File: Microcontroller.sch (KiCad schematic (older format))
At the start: 15 parts

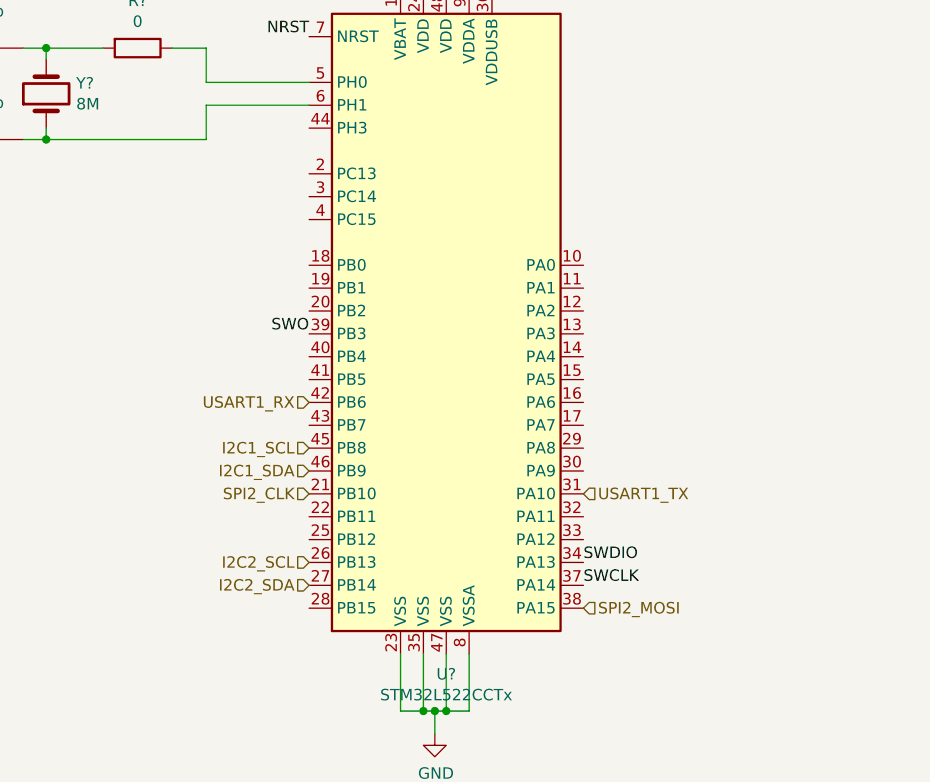
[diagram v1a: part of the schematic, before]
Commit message: added rj45 input
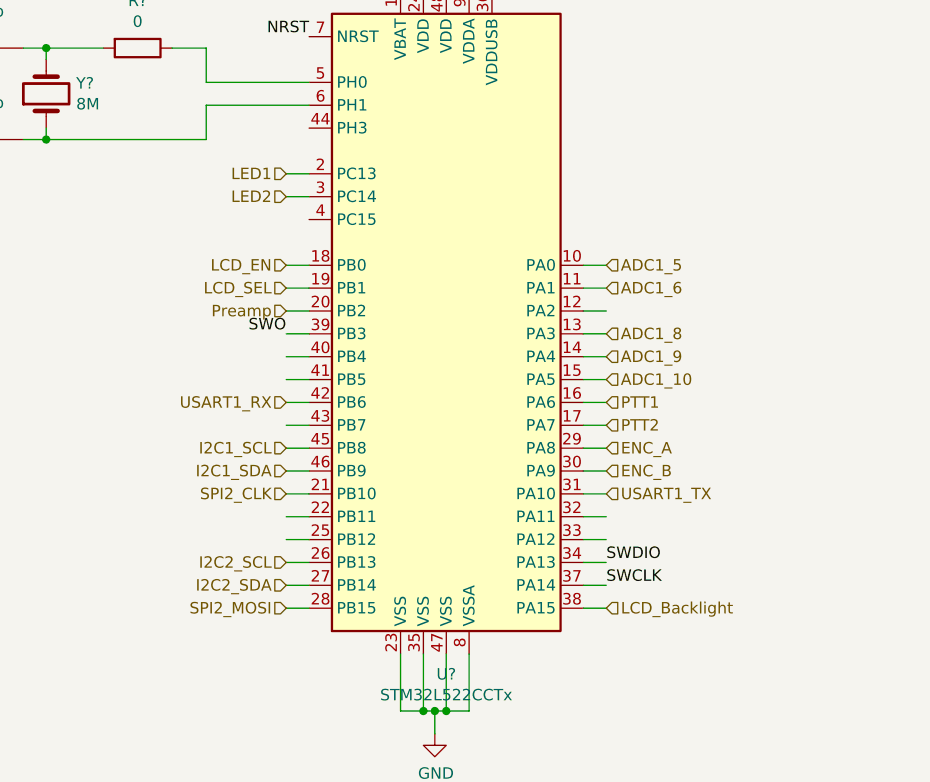
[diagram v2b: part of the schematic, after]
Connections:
- net labels added: ADC1_10, ADC1_5, ADC1_6, ADC1_8, ADC1_9, ENC_A, ENC_B, LCD_Backlight, LCD_EN, LCD_SEL, LED1, LED2, PTT1, PTT2, Preamp
- wire segments 61 -> 95
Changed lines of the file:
@@
 $Descr A4 11693 8268
 encoding utf-8
-Sheet 3 6
+Sheet 3 7
 Title ""
 Date ""
@@
 Text Label 4550 2350 2    50   ~ 0
 NRST
-Text Label 4550 3650 2    50   ~ 0
+Text Label 4450 3650 2    50   ~ 0
 SWO
-Text Label 5750 4650 0    50   ~ 0
+Text Label 5850 4650 0    50   ~ 0
 SWDIO
-Text Label 5750 4750 0    50   ~ 0
+Text Label 5850 4750 0    50   ~ 0
 SWCLK
 Text Label 9550 3150 2    50   ~ 0
@@
 Wire Wire Line
 	9450 3250 9550 3250
-Text HLabel 4550 4150 0    50   Input ~ 0
+Text HLabel 4450 4150 0    50   Input ~ 0
 I2C1_SCL
-Text HLabel 4550 4250 0    50   Input ~ 0
+Text HLabel 4450 4250 0    50   Input ~ 0
 I2C1_SDA
-Text HLabel 4550 4650 0    50   Input ~ 0
+Text HLabel 4450 4650 0    50   Input ~ 0
 I2C2_SCL
-Text HLabel 4550 4750 0    50   Input ~ 0
+Text HLabel 4450 4750 0    50   Input ~ 0
 I2C2_SDA
-Text HLabel 5750 4350 2    50   Input ~ 0
+Text HLabel 5850 4350 2    50   Input ~ 0
 USART1_TX
 Wire Wire Line
 	5350 1750 5350 2150
-Text HLabel 4550 3950 0    50   Input ~ 0
+Text HLabel 4450 3950 0    50   Input ~ 0
 USART1_RX
-Text HLabel 5750 4850 2    50   Input ~ 0
+Text HLabel 4450 4850 0    50   Input ~ 0
 SPI2_MOSI
-Text HLabel 4550 4350 0    50   Input ~ 0
+Text HLabel 4450 4350 0    50   Input ~ 0
 SPI2_CLK
 $Comp
@@
 Wire Wire Line
 	3400 2800 4100 2800
+Text HLabel 4450 2950 0    50   Input ~ 0
+LED1
+Text HLabel 4450 3050 0    50   Input ~ 0
+LED2
+Text HLabel 5850 4150 2    50   Input ~ 0
+ENC_A
+Text HLabel 5850 4250 2    50   Input ~ 0
+ENC_B
+Wire Wire Line
+	5750 4150 5850 4150
+Wire Wire Line
+	5750 4250 5850 4250
+Wire Wire Line
+	5750 4850 5850 4850
+Wire Wire Line
+	4450 3350 4550 3350
+Wire Wire Line
+	4450 3450 4550 3450
+Wire Wire Line
+	4450 3550 4550 3550
+Wire Wire Line
+	4450 3650 4550 3650
+Wire Wire Line
+	4450 3750 4550 3750
+Wire Wire Line
+	4450 3850 4550 3850
+Wire Wire Line
+	4450 3950 4550 3950
+Wire Wire Line
+	4450 4050 4550 4050
+Wire Wire Line
+	4450 4150 4550 4150
+Wire Wire Line
+	4450 4250 4550 4250
+Wire Wire Line
+	4450 4350 4550 4350
+Wire Wire Line
+	4450 4450 4550 4450
+Wire Wire Line
+	4450 4550 4550 4550
+Wire Wire Line
+	4450 4650 4550 4650
+Wire Wire Line
+	4450 4750 4550 4750
+Wire Wire Line
+	4450 4850 4550 4850
+Wire Wire Line
+	5850 3350 5750 3350
+Wire Wire Line
+	5850 3450 5750 3450
+Wire Wire Line
+	5850 3550 5750 3550
+Wire Wire Line
+	5850 3650 5750 3650
+Wire Wire Line
+	5850 3750 5750 3750
+Wire Wire Line
+	5850 3850 5750 3850
+Wire Wire Line
+	5850 3950 5750 3950
+Wire Wire Line
+	5850 4050 5750 4050
+Wire Wire Line
+	5850 4350 5750 4350
+Wire Wire Line
+	5850 4450 5750 4450
+Wire Wire Line
+	5850 4550 5750 4550
+Wire Wire Line
+	5850 4650 5750 4650
+Wire Wire Line
+	5850 4750 5750 4750
+Text HLabel 5850 3950 2    50   Input ~ 0
+PTT1
+Text HLabel 5850 4050 2    50   Input ~ 0
+PTT2
+Text HLabel 4450 3350 0    50   Input ~ 0
+LCD_EN
+Text HLabel 4450 3450 0    50   Input ~ 0
+LCD_SEL
+Text HLabel 5850 4850 2    50   Input ~ 0
+LCD_Backlight
+Text HLabel 5850 3350 2    50   Input ~ 0
+ADC1_5
+Text HLabel 5850 3450 2    50   Input ~ 0
+ADC1_6
+Text HLabel 5850 3650 2    50   Input ~ 0
+ADC1_8
+Text HLabel 5850 3750 2    50   Input ~ 0
+ADC1_9
+Text HLabel 5850 3850 2    50   Input ~ 0
+ADC1_10
+Wire Wire Line
+	4550 2950 4450 2950
+Wire Wire Line
+	4550 3050 4450 3050
+Text HLabel 4450 3550 0    50   Input ~ 0
+Preamp
 $EndSCHEMATC

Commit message: Ready for layout
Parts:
- removed R?: R, symbol AR2ISS:R
- added C?: 100n, symbol AR2ISS:C
- added JP?: Jumper_NC_Small, symbol Device:Jumper_NC_Small
- added R?: 10k, symbol AR2ISS:R
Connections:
- net labels added: AMP, CREL_A, CREL_B, C_NC, C_NO, PTT_Main, PTT_Sub, ROT_DOWN, ROT_LEFT, ROT_RIGHT, ROT_UP
- net labels removed: I2C2_SCL, I2C2_SDA, PTT1, PTT2
- wire segments 95 -> 105
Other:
- moved on the sheet: J?
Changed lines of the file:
@@
 $Descr A4 11693 8268
 encoding utf-8
-Sheet 3 7
+Sheet 7 9
 Title ""
 Date ""
@@
 	1    0    0    -1
 $EndComp
-$Comp
-L AR2ISS:R R?
-U 1 1 606DF993
-P 7550 1300
-F 0 "R?" H 7620 1346 50  0000 L CNN
-F 1 "R" H 7620 1255 50  0000 L CNN
-F 2 "" V 7480 1300 50  0001 C CNN
-F 3 "~" H 7550 1300 50  0001 C CNN
-	1    7550 1300
-	1    0    0    -1
-$EndComp
 Wire Wire Line
 	4950 1750 4950 2050
@@
 L Connector_Generic:Conn_02x03_Odd_Even J?
 U 1 1 606FEAF1
-P 9750 3150
-F 0 "J?" H 9800 3467 50  0000 C CNN
-F 1 "Conn_02x03_Odd_Even" H 9800 3376 50  0000 C CNN
-F 2 "" H 9750 3150 50  0001 C CNN
-F 3 "~" H 9750 3150 50  0001 C CNN
-	1    9750 3150
+P 8100 2800
+F 0 "J?" H 8150 3117 50  0000 C CNN
+F 1 "Conn_02x03_Odd_Even" H 8150 3026 50  0000 C CNN
+F 2 "" H 8100 2800 50  0001 C CNN
+F 3 "~" H 8100 2800 50  0001 C CNN
+	1    8100 2800
 	1    0    0    -1
 $EndComp
@@
 Text Label 5850 4750 0    50   ~ 0
 SWCLK
-Text Label 9550 3150 2    50   ~ 0
+Text Label 7900 2800 2    50   ~ 0
 NRST
-Text Label 10050 3250 0    50   ~ 0
+Text Label 8400 2900 0    50   ~ 0
 SWO
-Text Label 10050 3050 0    50   ~ 0
+Text Label 8400 2700 0    50   ~ 0
 SWDIO
-Text Label 10050 3150 0    50   ~ 0
+Text Label 8400 2800 0    50   ~ 0
 SWCLK
 $Comp
 L power:GND #PWR?
 U 1 1 60716775
-P 9450 3400
-F 0 "#PWR?" H 9450 3150 50  0001 C CNN
-F 1 "GND" H 9455 3227 50  0000 C CNN
-F 2 "" H 9450 3400 50  0001 C CNN
-F 3 "" H 9450 3400 50  0001 C CNN
-	1    9450 3400
+P 7800 3050
+F 0 "#PWR?" H 7800 2800 50  0001 C CNN
+F 1 "GND" H 7805 2877 50  0000 C CNN
+F 2 "" H 7800 3050 50  0001 C CNN
+F 3 "" H 7800 3050 50  0001 C CNN
+	1    7800 3050
 	1    0    0    -1
 $EndComp
@@
 L power:VDDA #PWR?
 U 1 1 60716CBB
-P 9450 2800
-F 0 "#PWR?" H 9450 2650 50  0001 C CNN
-F 1 "VDDA" H 9465 2973 50  0000 C CNN
-F 2 "" H 9450 2800 50  0001 C CNN
-F 3 "" H 9450 2800 50  0001 C CNN
-	1    9450 2800
-	1    0    0    -1
-$EndComp
-Wire Wire Line
-	9450 2800 9450 3050
-Wire Wire Line
-	9450 3050 9550 3050
-Wire Wire Line
-	9450 3400 9450 3250
-Wire Wire Line
-	9450 3250 9550 3250
+P 7800 2450
+F 0 "#PWR?" H 7800 2300 50  0001 C CNN
+F 1 "VDDA" H 7815 2623 50  0000 C CNN
+F 2 "" H 7800 2450 50  0001 C CNN
+F 3 "" H 7800 2450 50  0001 C CNN
+	1    7800 2450
+	1    0    0    -1
+$EndComp
+Wire Wire Line
+	7800 2450 7800 2700
+Wire Wire Line
+	7800 2700 7900 2700
+Wire Wire Line
+	7800 3050 7800 2900
+Wire Wire Line
+	7800 2900 7900 2900
 Text HLabel 4450 4150 0    50   Input ~ 0
 I2C1_SCL
 Text HLabel 4450 4250 0    50   Input ~ 0
 I2C1_SDA
-Text HLabel 4450 4650 0    50   Input ~ 0
-I2C2_SCL
-Text HLabel 4450 4750 0    50   Input ~ 0
-I2C2_SDA
 Text HLabel 5850 4350 2    50   Input ~ 0
 USART1_TX
@@
 	5850 4750 5750 4750
 Text HLabel 5850 3950 2    50   Input ~ 0
-PTT1
+PTT_Main
 Text HLabel 5850 4050 2    50   Input ~ 0
-PTT2
+PTT_Sub
 Text HLabel 4450 3350 0    50   Input ~ 0
 LCD_EN
@@
 Text HLabel 4450 3550 0    50   Input ~ 0
 Preamp
+Text HLabel 4450 4450 0    50   Input ~ 0
+ROT_UP
+Text HLabel 4450 4550 0    50   Input ~ 0
+ROT_DOWN
+Text HLabel 4450 4650 0    50   Input ~ 0
+ROT_LEFT
+Text HLabel 4450 4750 0    50   Input ~ 0
+ROT_RIGHT
+Text HLabel 5850 4450 2    50   Input ~ 0
+CREL_A
+Text HLabel 5850 4550 2    50   Input ~ 0
+CREL_B
+Text HLabel 4450 4050 0    50   Input ~ 0
+AMP
+Text HLabel 4450 3750 0    50   Input ~ 0
+C_NO
+Text HLabel 4450 3850 0    50   Input ~ 0
+C_NC
+$Comp
+L AR2ISS:R R?
+U 1 1 609716B8
+P 7400 2600
+F 0 "R?" V 7193 2600 50  0000 C CNN
+F 1 "10k" V 7284 2600 50  0000 C CNN
+F 2 "" V 7330 2600 50  0001 C CNN
+F 3 "~" H 7400 2600 50  0001 C CNN
+	1    7400 2600
+	-1   0    0    1
+$EndComp
+Wire Wire Line
+	7900 2800 7400 2800
+Wire Wire Line
+	7400 2800 7400 2750
+$Comp
+L power:+3V3 #PWR?
+U 1 1 60974B50
+P 7400 2350
+F 0 "#PWR?" H 7400 2200 50  0001 C CNN
+F 1 "+3V3" H 7415 2523 50  0000 C CNN
+F 2 "" H 7400 2350 50  0001 C CNN
+F 3 "" H 7400 2350 50  0001 C CNN
+	1    7400 2350
+	1    0    0    -1
+$EndComp
+Wire Wire Line
+	7400 2350 7400 2450
+Wire Wire Line
+	4550 2750 4150 2750
+Wire Wire Line
+	4150 2750 4150 2850
+Wire Wire Line
+	4150 2850 3900 2850
+Wire Wire Line
+	3900 2850 3900 2950
+$Comp
+L power:GND #PWR?
+U 1 1 6097B5D1
+P 3900 3200
+F 0 "#PWR?" H 3900 2950 50  0001 C CNN
+F 1 "GND" V 3905 3072 50  0000 R CNN
+F 2 "" H 3900 3200 50  0001 C CNN
+F 3 "" H 3900 3200 50  0001 C CNN
+	1    3900 3200
+	-1   0    0    -1
+$EndComp
+$Comp
+L AR2ISS:C C?
+U 1 1 6097BB40
+P 7400 3000
+F 0 "C?" H 7285 2954 50  0000 R CNN
+F 1 "100n" H 7285 3045 50  0000 R CNN
+F 2 "" H 7438 2850 50  0001 C CNN
+F 3 "~" H 7400 3000 50  0001 C CNN
+	1    7400 3000
+	-1   0    0    1
+$EndComp
+Wire Wire Line
+	7400 2800 7400 2850
+Connection ~ 7400 2800
+$Comp
+L power:GND #PWR?
+U 1 1 6097F29C
+P 7400 3250
+F 0 "#PWR?" H 7400 3000 50  0001 C CNN
+F 1 "GND" H 7405 3077 50  0000 C CNN
+F 2 "" H 7400 3250 50  0001 C CNN
+F 3 "" H 7400 3250 50  0001 C CNN
+	1    7400 3250
+	1    0    0    -1
+$EndComp
+Wire Wire Line
+	7400 3150 7400 3250
+$Comp
+L Device:Jumper_NC_Small JP?
+U 1 1 60982DC3
+P 3900 3050
+F 0 "JP?" V 3946 3003 50  0000 R CNN
+F 1 "Jumper_NC_Small" H 4050 3200 50  0000 R CNN
+F 2 "" H 3900 3050 50  0001 C CNN
+F 3 "~" H 3900 3050 50  0001 C CNN
+	1    3900 3050
+	0    -1   -1   0
+$EndComp
+Wire Wire Line
+	3900 3150 3900 3200
 $EndSCHEMATC

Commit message: first layout
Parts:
- C19, C20, C21, C22, C23, C24, C25, C26, C27, C28: renamed from C?; footprint (none) -> Capacitor_SMD:C_0603_1608Metric
- J5: renamed from J?; footprint (none) -> Connector_IDC:IDC-Header_2x03_P2.54mm_Vertical
- JP1: renamed from JP?; footprint (none) -> Jumper:SolderJumper-2_P1.3mm_Bridged_RoundedPad1.0x1.5mm
- L2: renamed from L?; footprint (none) -> Inductor_SMD:L_0603_1608Metric
- R41, R42: renamed from R?; footprint (none) -> Resistor_SMD:R_0603_1608Metric
- Y1: renamed from Y?; footprint (none) -> Crystal:Crystal_SMD_5032-2Pin_5.0x3.2mm_HandSoldering
- gave numbers to parts that had none: 1
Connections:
- net +3V3: now also J5.1 (Pin_1)
- net LED1: now also U12.3 (PC14); no longer U12.2 (PC13)
- net LED2: now also U12.2 (PC13); no longer U12.3 (PC14)
- net PTT_Main: now also U12.17 (PA7); no longer U12.16 (PA6)
- net PTT_Sub: now also U12.16 (PA6); no longer U12.17 (PA7)
- net VDDA: now also U12.9 (VDDA); no longer J5.1 (Pin_1)

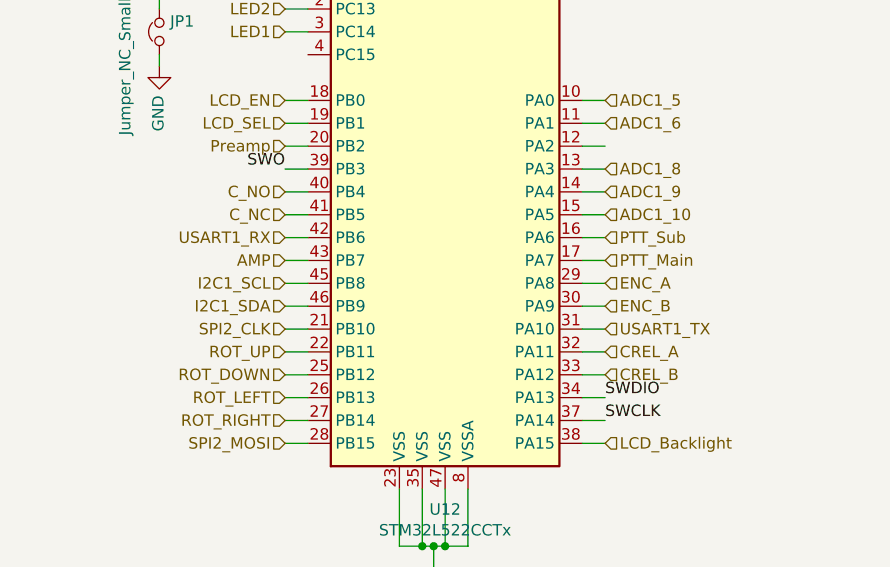
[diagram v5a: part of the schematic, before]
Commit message: uart rx tx reversed
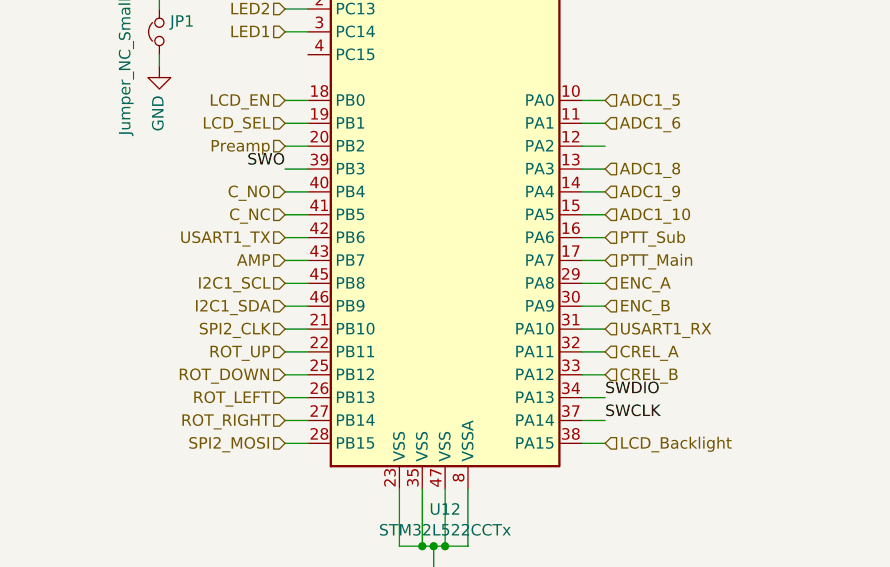
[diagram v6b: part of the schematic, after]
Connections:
- net USART1_RX: now also U12.31 (PA10); no longer U12.42 (PB6)
- net USART1_TX: now also U12.42 (PB6); no longer U12.31 (PA10)
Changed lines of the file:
@@
 I2C1_SDA
 Text HLabel 5850 4350 2    50   Input ~ 0
-USART1_TX
+USART1_RX
 Wire Wire Line
 	5350 1750 5350 2150
 Text HLabel 4450 3950 0    50   Input ~ 0
-USART1_RX
+USART1_TX
 Text HLabel 4450 4850 0    50   Input ~ 0
 SPI2_MOSI
